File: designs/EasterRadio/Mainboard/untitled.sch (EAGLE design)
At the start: 7 parts

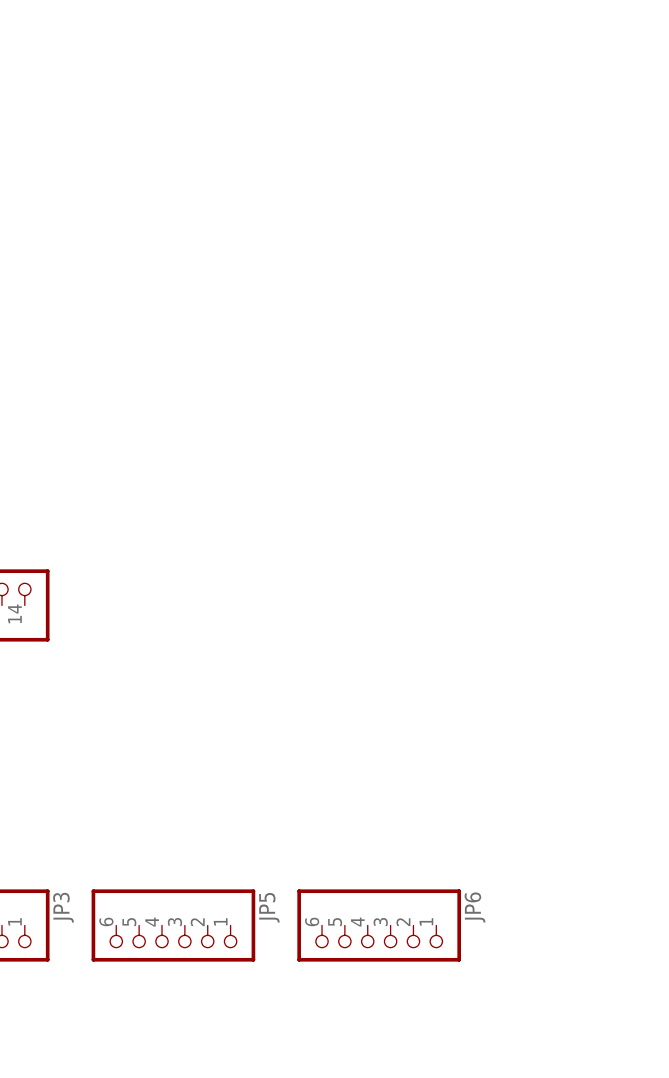
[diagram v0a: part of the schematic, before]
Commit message: added mainboard layout and new 3.5mm jack
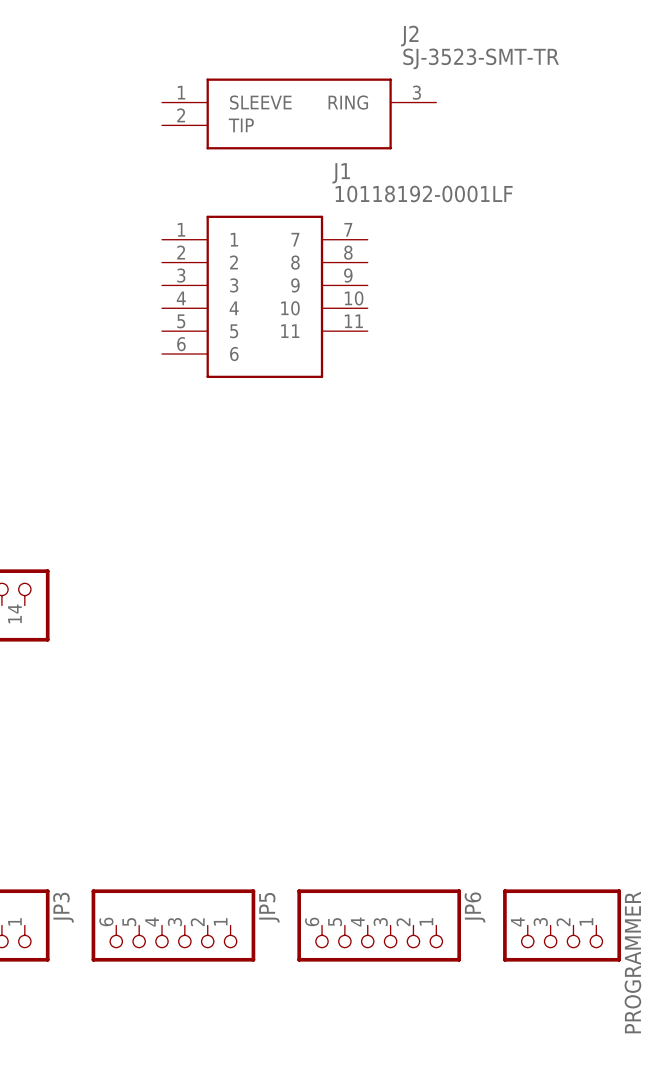
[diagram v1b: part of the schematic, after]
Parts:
- added J1: 10118192-0001LF, MouserUseful:10118192-0001LF
- added J2: SJ-3523-SMT-TR, MouserUseful:SJ-3523-SMT-TR
- added PROGRAMMER: (no value), pinhead:PINHD-1X4
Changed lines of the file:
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@@
 <layer number="97" name="Info" color="7" fill="1" visible="yes" active="yes"/>
 <layer number="98" name="Guide" color="6" fill="1" visible="yes" active="yes"/>
+<layer number="99" name="SpiceOrder" color="5" fill="1" visible="yes" active="yes"/>
 </layers>
 <schematic xreflabel="%F%N/%S.%C%R" xrefpart="/%S.%C%R">
@@
 <part name="JP6" library="pinhead" library_urn="urn:adsk.eagle:library:325" deviceset="PINHD-1X6" device="" package3d_urn="urn:adsk.eagle:package:22472/2"/>
 <part name="JP7" library="pinhead" library_urn="urn:adsk.eagle:library:325" deviceset="PINHD-1X8" device="" package3d_urn="urn:adsk.eagle:package:22409/2"/>
+<part name="J1" library="MouserUseful" deviceset="10118192-0001LF" device=""/>
+<part name="PROGRAMMER" library="pinhead" library_urn="urn:adsk.eagle:library:325" deviceset="PINHD-1X4" device="" package3d_urn="urn:adsk.eagle:package:22407/2"/>
+<part name="J2" library="MouserUseful" deviceset="SJ-3523-SMT-TR" device=""/>
 </parts>
 <sheets>
@@
 <attribute name="VALUE" x="5.08" y="44.45" size="1.778" layer="96" rot="R270"/>
 </instance>
+<instance part="J1" gate="G$1" x="111.76" y="91.44" smashed="yes">
+<attribute name="NAME" x="130.81" y="99.06" size="1.778" layer="95" align="center-left"/>
+<attribute name="VALUE" x="130.81" y="96.52" size="1.778" layer="96" align="center-left"/>
+</instance>
+<instance part="PROGRAMMER" gate="A" x="154.94" y="12.7" smashed="yes" rot="R270">
+<attribute name="NAME" x="163.195" y="19.05" size="1.778" layer="95" rot="R270"/>
+<attribute name="VALUE" x="147.32" y="19.05" size="1.778" layer="96" rot="R270"/>
+</instance>
+<instance part="J2" gate="G$1" x="111.76" y="106.68" smashed="yes">
+<attribute name="NAME" x="138.43" y="114.3" size="1.778" layer="95" align="center-left"/>
+<attribute name="VALUE" x="138.43" y="111.76" size="1.778" layer="96" align="center-left"/>
+</instance>
 </instances>

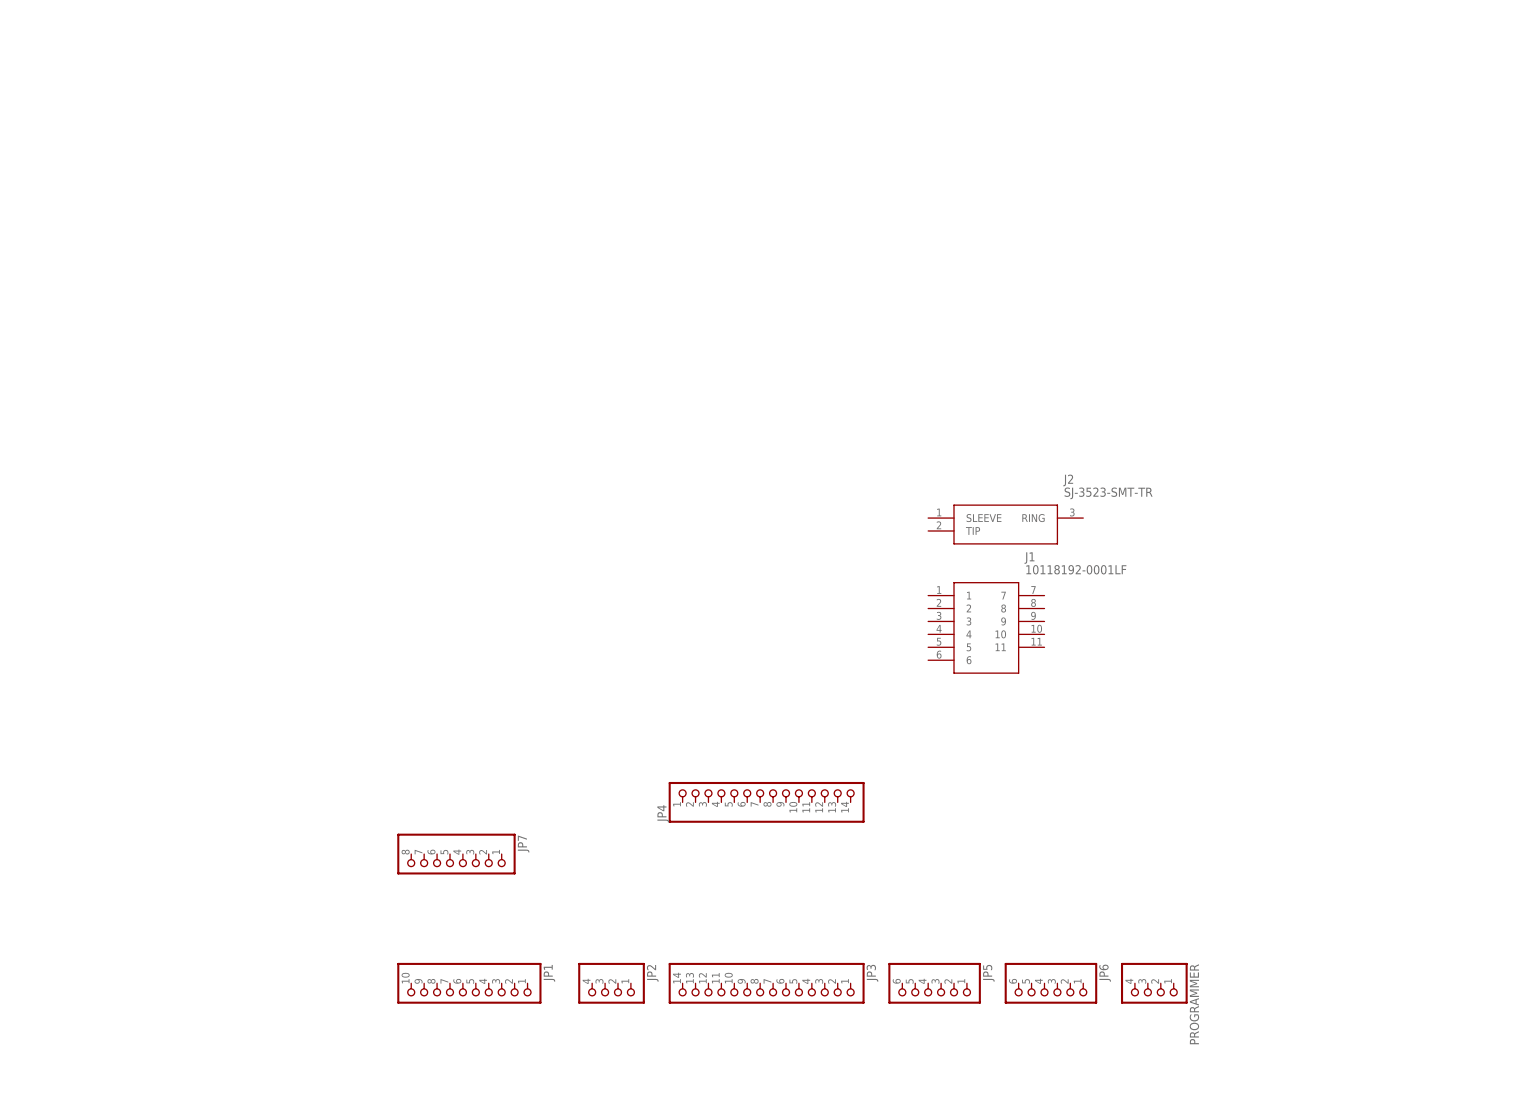
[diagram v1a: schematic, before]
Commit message: added more stuff to pcb main for radio
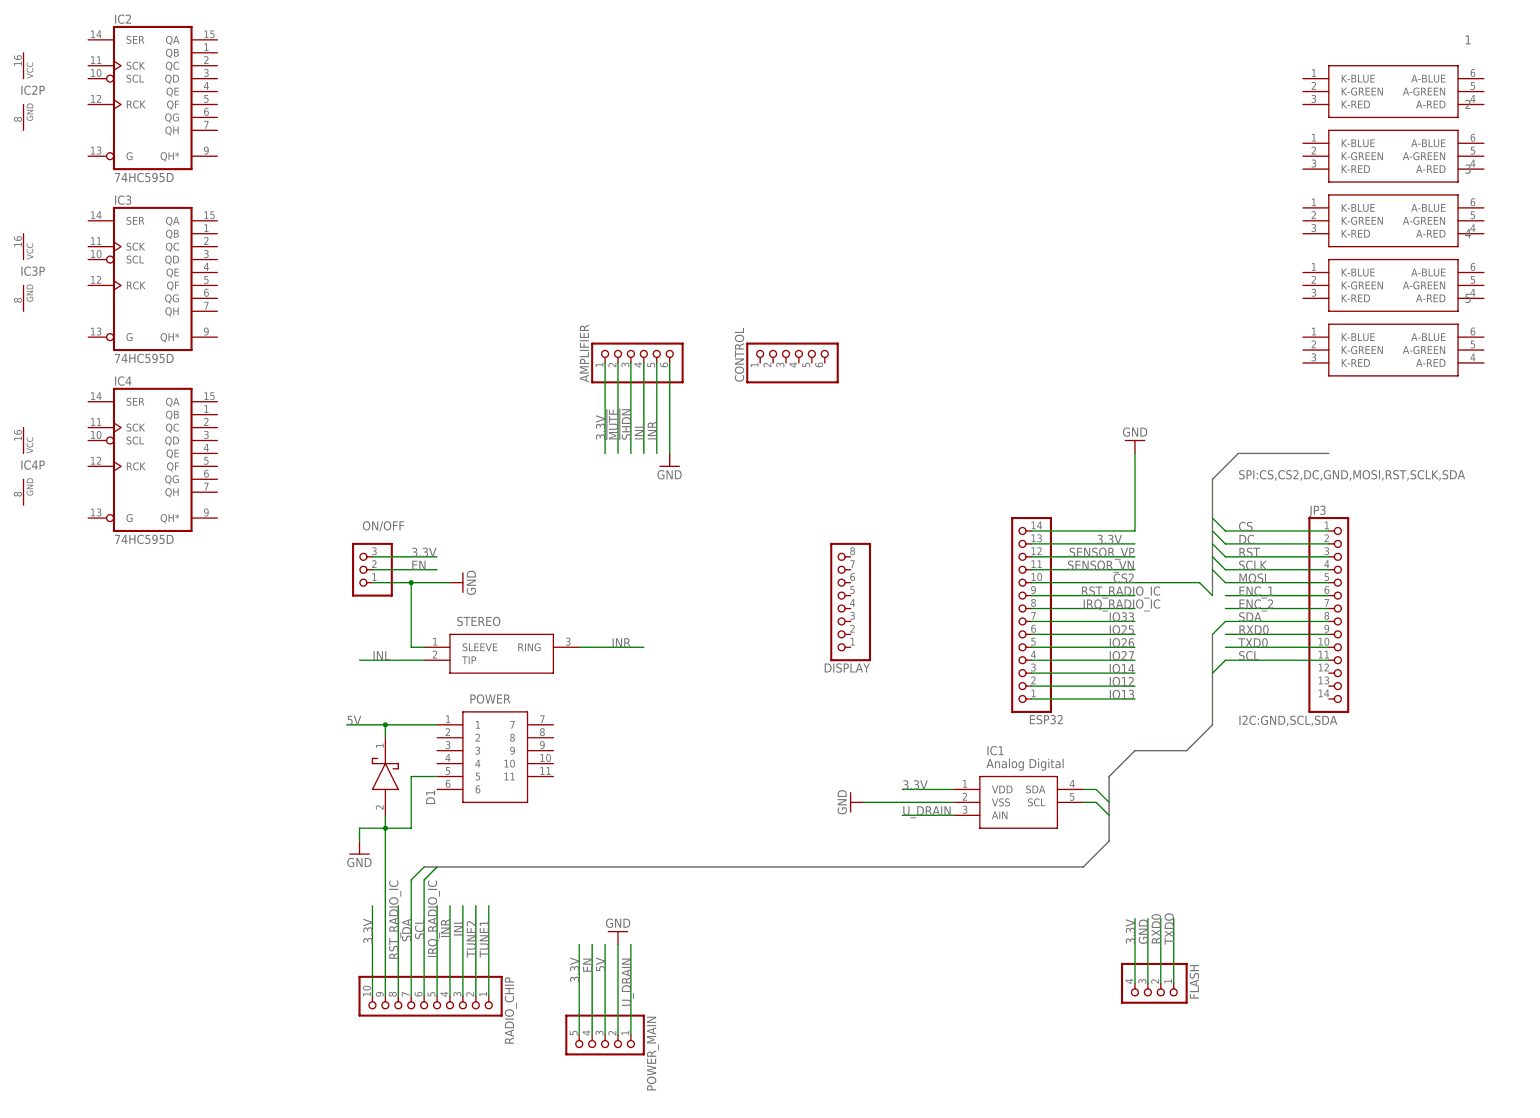
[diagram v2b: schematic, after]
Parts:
- removed J1: 10118192-0001LF, MouserUseful:10118192-0001LF
- removed J2: SJ-3523-SMT-TR, MouserUseful:SJ-3523-SMT-TR
- removed JP1: (no value), pinhead:PINHD-1X10
- removed JP2: (no value), pinhead:PINHD-1X4
- removed JP4: (no value), pinhead:PINHD-1X14
- removed JP5, JP6: (no value), pinhead:PINHD-1X6
- removed JP7: (no value), pinhead:PINHD-1X8
- added 1, 2, 3, 4, 5: CLY6D-FKC-CK1N1D1BB7D3D3, MouserUseful:CLY6D-FKC-CK1N1D1BB7D3D3
- added AMPLIFIER, CONTROL: (no value), pinhead:PINHD-1X6
- added D1: LSM115JE3_TR13, CommonParts:LSM115JE3_TR13
- added DISPLAY: (no value), pinhead:PINHD-1X8
- added ESP32: (no value), pinhead:PINHD-1X14
- added IC1: Analog Digital, MouserUseful:MCP3221A6T-E_OTVAO
- added IC2, IC3, IC4: 74HC595D, NixieTube:74HC595D
- added ON/OFF: (no value), pinhead:PINHD-1X3
- added POWER: 10118192-0001LF, MouserUseful:10118192-0001LF
- added POWER_MAIN: (no value), pinhead:PINHD-1X5
- added RADIO_CHIP: (no value), pinhead:PINHD-1X10
- added STEREO: SJ-3523-SMT-TR, MouserUseful:SJ-3523-SMT-TR
- renumbered PROGRAMMER to FLASH
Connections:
- new net !MUTE: AMPLIFIER.2
- new net !SHDN: AMPLIFIER.3
- new net 3.3V: AMPLIFIER.1, ESP32.13, FLASH.4, IC1.VDD, ON/OFF.3, POWER_MAIN.5, RADIO_CHIP.10
- new net 5V: D1.K, POWER.1, POWER_MAIN.3
- new net CS: JP3.1
- new net CS2: ESP32.10
- new net DC: JP3.2
- new net EN: ON/OFF.2, POWER_MAIN.4
- new net ENC_1: JP3.6
- new net ENC_2: JP3.7
- new net GND: AMPLIFIER.6, D1.A, ESP32.14, FLASH.3, IC1.VSS, ON/OFF.1, POWER.5, POWER_MAIN.2, RADIO_CHIP.9, STEREO.SLEEVE
- new net INL: AMPLIFIER.4, RADIO_CHIP.3, STEREO.TIP
- new net INR: AMPLIFIER.5, RADIO_CHIP.4, STEREO.RING
- new net IO12: ESP32.2
- new net IO13: ESP32.1
- new net IO14: ESP32.3
- new net IO25: ESP32.6
- new net IO26: ESP32.5
- new net IO27: ESP32.4
- new net IO33: ESP32.7
- new net IRQ_RADIO_IC: ESP32.8, RADIO_CHIP.5
- new net MOSI: JP3.5
- new net RST: JP3.3
- new net RST_RADIO_IC: ESP32.9, RADIO_CHIP.8
- new net RXD0: FLASH.2, JP3.9
- new net SCL: IC1.SCL, JP3.11, RADIO_CHIP.6
- new net SCLK: JP3.4
- new net SDA: IC1.SDA, JP3.8, RADIO_CHIP.7
- new net SENSOR_VN: ESP32.11
- new net SENSOR_VP: ESP32.12
- new net TUNE1: RADIO_CHIP.1
- new net TUNE2: RADIO_CHIP.2
- new net TXD0: JP3.10
- new net TXDO: FLASH.1
- new net U_DRAIN: IC1.AIN, POWER_MAIN.1
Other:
- moved on the sheet: JP3

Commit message: started board routing
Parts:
- added D10, D11, D12, D13, D14, D15, D16, D17, D18, D19, D2, D20, D21, D22, D23, D24, D25, D26, D3, D4, D5, D6, D7, D8, D9: PESD3V3L2BT,215, MouserUseful:PESD3V3L2BT,215
- added GPIOS: (no value), pinhead:PINHD-1X4
- POWER: value 10118192-0001LF -> KMMX-BSMT35S-B30TR; device MouserUseful:10118192-0001LF -> MouserUseful:KMMX-BSMT35S-B30TR
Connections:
- removed net IO25: ESP32.6
- removed net IO26: ESP32.5
- removed net IO33: ESP32.7
- new net DS: D22.CATHODE_2, ESP32.7, IC2A.SER
- new net ENC_A: CONTROL.4, D2.CATHODE_2
- new net ENC_B: CONTROL.5, D2.CATHODE_1
- new net N$10: 2.A-RED, IC2A.QD
- new net N$11: 2.A-GREEN, IC2A.QE
- new net N$12: 2.A-BLUE, IC2A.QF
- new net N$13: 3.A-RED, IC3A.QA
- new net N$14: 3.A-GREEN, IC3A.QB
- new net N$15: 4.A-RED, IC3A.QD
- new net N$16: 4.A-GREEN, IC3A.QE
- new net N$17: IC2A.QH*, IC3A.SER
- new net N$18: 5.A-RED, IC4A.QA
- new net N$19: 5.A-GREEN, IC4A.QB
- new net N$21: IC3A.QH*, IC4A.SER
- new net N$3: 3.A-BLUE, IC3A.QC
- new net N$4: 5.A-BLUE, IC4A.QC
- new net N$6: 4.A-BLUE, IC3A.QF
- new net N$7: 1.A-RED, IC2A.QA
- new net N$8: 1.A-GREEN, IC2A.QB
- new net N$9: 1.A-BLUE, IC2A.QC
- new net SHCP: D23.CATHODE_1, ESP32.6, IC2A.SCK, IC3A.SCK, IC4A.SCK
- new net STCP: D23.CATHODE_2, ESP32.5, IC2A.RCK, IC3A.RCK, IC4A.RCK
- net !MUTE: now also D6.CATHODE_1
- net !SHDN: now also D5.CATHODE_2
- net 3.3V: now also CONTROL.3, D14.CATHODE_1, D3.CATHODE_1, DISPLAY.8, IC2A.SCL, IC2P.VCC, IC3A.SCL, IC3P.VCC, IC4A.SCL, IC4P.VCC
- net CS: now also D15.CATHODE_1, DISPLAY.4
- net DC: now also D15.CATHODE_2, DISPLAY.3
- net EN: now also D14.CATHODE_2, D7.CATHODE_2
- net ENC_1: now also D17.CATHODE_2
- net ENC_2: now also D18.CATHODE_1
- net GND: now also 1.K-BLUE, 1.K-GREEN, 1.K-RED, 2.K-BLUE, 2.K-GREEN, 2.K-RED, 3.K-BLUE, 3.K-GREEN, 3.K-RED, 4.K-BLUE, 4.K-GREEN, 4.K-RED, 5.K-BLUE, 5.K-GREEN, 5.K-RED, CONTROL.6, D10.DOUBLE_CATHODE, D11.DOUBLE_CATHODE, D12.DOUBLE_CATHODE, D13.DOUBLE_CATHODE, D14.DOUBLE_CATHODE, D15.DOUBLE_CATHODE, D16.DOUBLE_CATHODE, D17.DOUBLE_CATHODE, D18.DOUBLE_CATHODE, D19.DOUBLE_CATHODE, D2.DOUBLE_CATHODE, D20.DOUBLE_CATHODE, D21.DOUBLE_CATHODE, D22.DOUBLE_CATHODE, D23.DOUBLE_CATHODE, D24.DOUBLE_CATHODE, D25.DOUBLE_CATHODE, D26.DOUBLE_CATHODE, D3.DOUBLE_CATHODE, D4.DOUBLE_CATHODE, D5.DOUBLE_CATHODE, D6.DOUBLE_CATHODE, D7.DOUBLE_CATHODE, D8.DOUBLE_CATHODE, D9.DOUBLE_CATHODE, DISPLAY.7, IC2A.G, IC2P.GND, IC3A.G, IC3P.GND, IC4A.G, IC4P.GND
- net INL: now also D12.CATHODE_2, D5.CATHODE_1, D9.CATHODE_1
- net INR: now also D12.CATHODE_1, D4.CATHODE_2, D9.CATHODE_2
- net IO12: now also D25.CATHODE_1, GPIOS.3
- net IO13: now also D25.CATHODE_2, GPIOS.4
- net IO14: now also D24.CATHODE_2, GPIOS.2
- net IO27: now also D24.CATHODE_1, GPIOS.1
- net IRQ_RADIO_IC: now also D11.CATHODE_2, D21.CATHODE_2
- net MOSI: now also D17.CATHODE_1, DISPLAY.6
- net RST: now also D16.CATHODE_1, DISPLAY.2
- net RST_RADIO_IC: now also D21.CATHODE_1
- net RXD0: now also D19.CATHODE_1, D8.CATHODE_1
- net SCL: now also D11.CATHODE_1, D20.CATHODE_1
- net SCLK: now also D16.CATHODE_2, DISPLAY.5
- net SDA: now also D10.CATHODE_2, D18.CATHODE_2
- net SENSOR_VN: now also D26.CATHODE_2
- net SENSOR_VP: now also D26.CATHODE_1
- net TUNE1: now also CONTROL.1, D13.CATHODE_2, D4.CATHODE_1
- net TUNE2: now also CONTROL.2, D13.CATHODE_1, D3.CATHODE_2
- net TXD0: now also D19.CATHODE_2
- net TXDO: now also D8.CATHODE_2
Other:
- moved on the sheet: 1, 2, 3, 4, 5, AMPLIFIER, CONTROL, D1, DISPLAY, ESP32, FLASH, IC1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
